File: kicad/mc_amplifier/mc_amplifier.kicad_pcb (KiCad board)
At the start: 2 copper layers, 35 x 13 mm, 19 parts

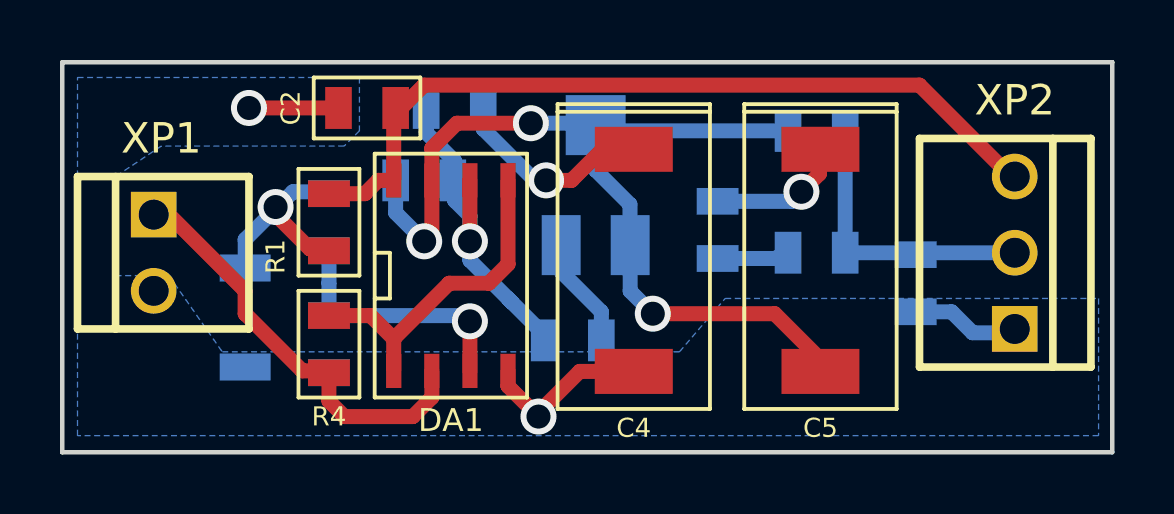
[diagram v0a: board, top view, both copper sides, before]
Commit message: Добавил новую ревизию схемы mc_amplifier (rev_2).
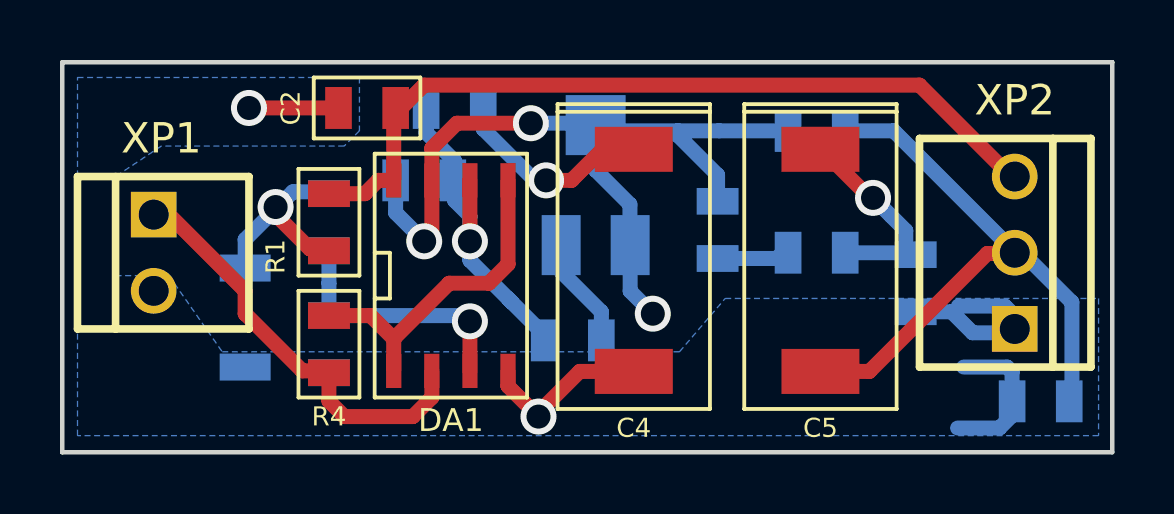
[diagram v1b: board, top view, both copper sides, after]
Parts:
- added R11: 47 к, IWsmd_case:SMD0805, B.Cu at (204.1, 128.1)
- R2, R4: value 5.1 к -> 5.1 к 1%
- R6: value 50 к -> 100 к
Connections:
- C5 pad 2: Net-(C3-Pad1) -> Net-(C5-Pad2)
- R10 pad 2: Net-(R10-Pad2) -> Net-(C5-Pad2)
- R7 pad 1: Net-(C5-Pad1) -> Net-(C3-Pad1)
- R8 pad 2: Net-(R10-Pad2) -> Net-(C5-Pad1)
- R9 pad 1: Net-(R10-Pad2) -> Net-(C5-Pad1)
- XP2 pad 2: Net-(R10-Pad2) -> Net-(C5-Pad2)
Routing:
- net Net-(C5-Pad2): track 0.00 -> 21.5 mm
- net Net-(R10-Pad2): track 9.59 -> 0.00 mm
- net /GND: track 12.4 -> 20.0 mm
- net Net-(C3-Pad1): track 31.3 -> 27.6 mm
- net Net-(C5-Pad1): track 4.79 -> 6.91 mm

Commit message: Проверил работоспособность платы mc_amplifier ver_1.
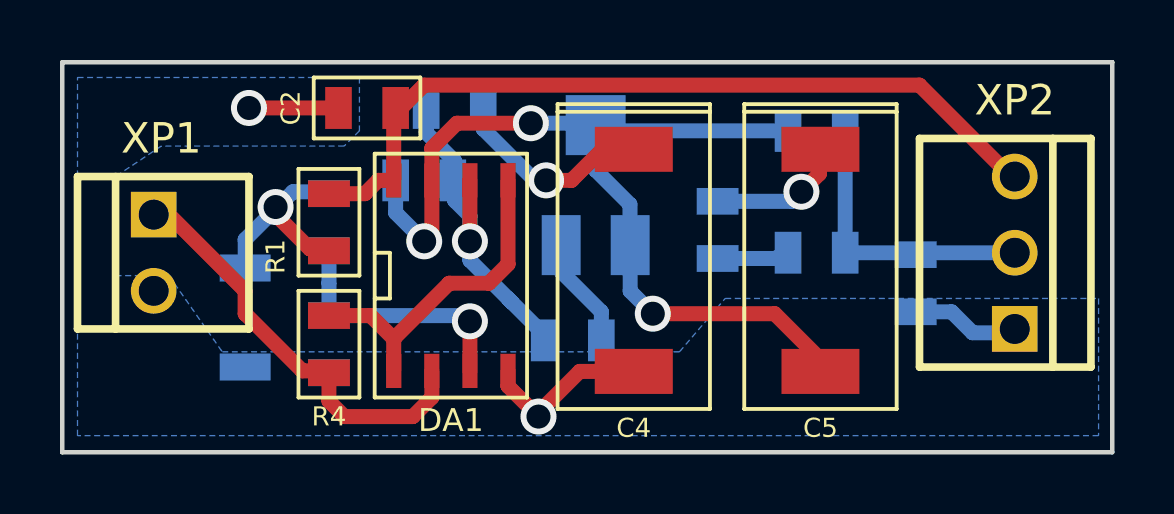
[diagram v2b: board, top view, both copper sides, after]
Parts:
- removed R11: 47 к, IWsmd_case:SMD0805
- R2, R4: value 5.1 к 1% -> 5.1 к
- R6: value 100 к -> 50 к
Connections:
- C5 pad 2: Net-(C5-Pad2) -> Net-(C3-Pad1)
- R10 pad 2: Net-(C5-Pad2) -> Net-(R10-Pad2)
- R7 pad 1: Net-(C3-Pad1) -> Net-(C5-Pad1)
- R8 pad 2: Net-(C5-Pad1) -> Net-(R10-Pad2)
- R9 pad 1: Net-(C5-Pad1) -> Net-(R10-Pad2)
- XP2 pad 2: Net-(C5-Pad2) -> Net-(R10-Pad2)
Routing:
- net Net-(C5-Pad2): track 21.5 -> 0.00 mm
- net Net-(R10-Pad2): track 0.00 -> 9.59 mm
- net /GND: track 20.0 -> 12.4 mm
- net Net-(C3-Pad1): track 27.6 -> 31.3 mm
- net Net-(C5-Pad1): track 6.91 -> 4.79 mm
